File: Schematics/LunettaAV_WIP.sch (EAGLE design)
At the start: 9 parts

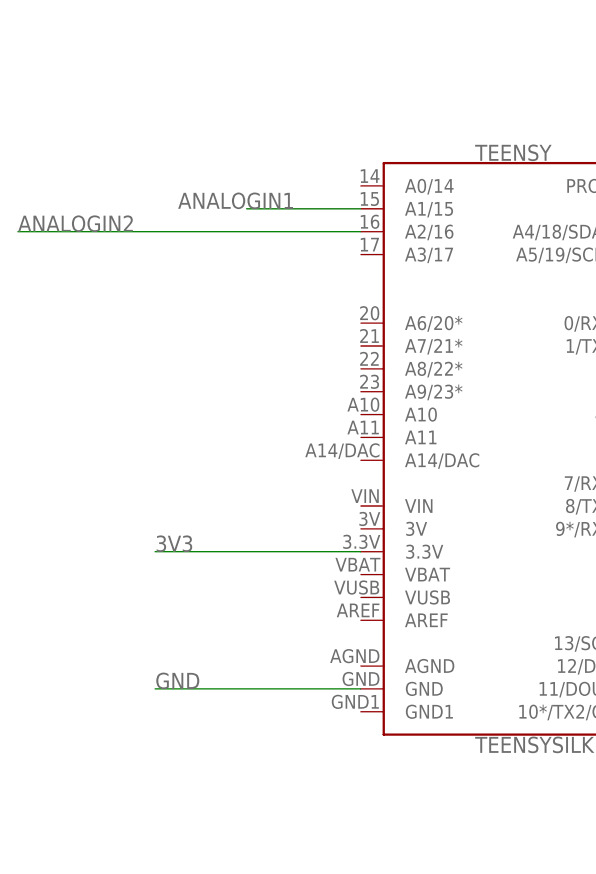
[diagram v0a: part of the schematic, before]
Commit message: fix analog input pins
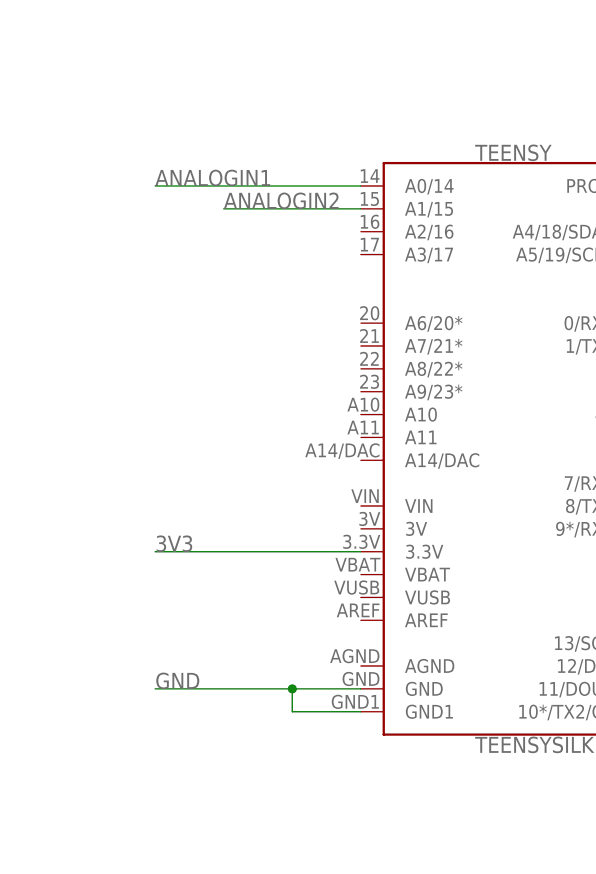
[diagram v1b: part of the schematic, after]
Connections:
- net ANALOGIN1: now also TEENSY.A0/14; no longer TEENSY.A1/15
- net ANALOGIN2: now also TEENSY.A1/15; no longer TEENSY.A2/16
- net GND: now also TEENSY.GND1
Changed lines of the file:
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@@
 <segment>
 <pinref part="TEENSY" gate="G$1" pin="GND"/>
-<wire x1="15.24" y1="25.4" x2="-7.62" y2="25.4" width="0.1524" layer="91"/>
+<wire x1="15.24" y1="25.4" x2="7.62" y2="25.4" width="0.1524" layer="91"/>
 <label x="-7.62" y="25.4" size="1.778" layer="95"/>
+<pinref part="TEENSY" gate="G$1" pin="GND1"/>
+<wire x1="7.62" y1="25.4" x2="-7.62" y2="25.4" width="0.1524" layer="91"/>
+<wire x1="15.24" y1="22.86" x2="7.62" y2="22.86" width="0.1524" layer="91"/>
+<wire x1="7.62" y1="22.86" x2="7.62" y2="25.4" width="0.1524" layer="91"/>
+<junction x="7.62" y="25.4"/>
 </segment>
 <segment>
@@
 <net name="ANALOGIN1" class="0">
 <segment>
-<pinref part="TEENSY" gate="G$1" pin="A1/15"/>
-<wire x1="15.24" y1="78.74" x2="2.54" y2="78.74" width="0.1524" layer="91"/>
-<label x="-5.08" y="78.74" size="1.778" layer="95"/>
-</segment>
-<segment>
 <pinref part="SPEEDER" gate="G$1" pin="S"/>
 <wire x1="73.66" y1="10.16" x2="73.66" y2="25.4" width="0.1524" layer="91"/>
 <label x="73.66" y="25.4" size="1.778" layer="95"/>
 </segment>
+<segment>
+<pinref part="TEENSY" gate="G$1" pin="A0/14"/>
+<wire x1="15.24" y1="81.28" x2="-7.62" y2="81.28" width="0.1524" layer="91"/>
+<label x="-7.62" y="81.28" size="1.778" layer="95"/>
+</segment>
 </net>
 <net name="ANALOGIN2" class="0">
-<segment>
-<pinref part="TEENSY" gate="G$1" pin="A2/16"/>
-<wire x1="15.24" y1="76.2" x2="-22.86" y2="76.2" width="0.1524" layer="91"/>
-<label x="-22.86" y="76.2" size="1.778" layer="95"/>
-</segment>
 <segment>
 <pinref part="SCALER" gate="G$1" pin="S"/>
@@
 <label x="106.68" y="25.4" size="1.778" layer="95"/>
 </segment>
+<segment>
+<pinref part="TEENSY" gate="G$1" pin="A1/15"/>
+<wire x1="15.24" y1="78.74" x2="0" y2="78.74" width="0.1524" layer="91"/>
+<label x="0" y="78.74" size="1.778" layer="95"/>
+</segment>
 </net>

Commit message: Add 358 and 4046 sections
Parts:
- added C1: 1uF, SparkFun-Capacitors:10NF-PTH-10MM-10000V-1-%
- added IC1: 4046N, 40xx:4046N
- added R4: 10K, MusicThingModular:RESISTOR7MM
- added TNSY5VIN: (no value), SparkFun-Retired:JUMPER-2PTH
- added U1: LM358, SparkFun-IC-Amplifiers:LM358
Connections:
- new net 5V: TNSY5VIN.1
- new net 9V: IC1P.VDD, U1G3.P$V+
- new net N$1: TEENSY.VIN, TNSY5VIN.2
- new net N$2: C1.2, IC1A.CX@2
- new net N$5: C1.1, IC1A.CX@1
- new net N$6: IC1A.R1, R4.2
- new net PLLCLOCK: IC1A.VCOOUT
- new net SPEEDYBUFF: IC1A.VCOIN, U1G1.-IN, U1G1.OUT
- net ANALOGIN1: now also U1G1.+IN
- net GND: now also IC1A.INH, IC1P.VSS, R4.1, U1G3.P$V-

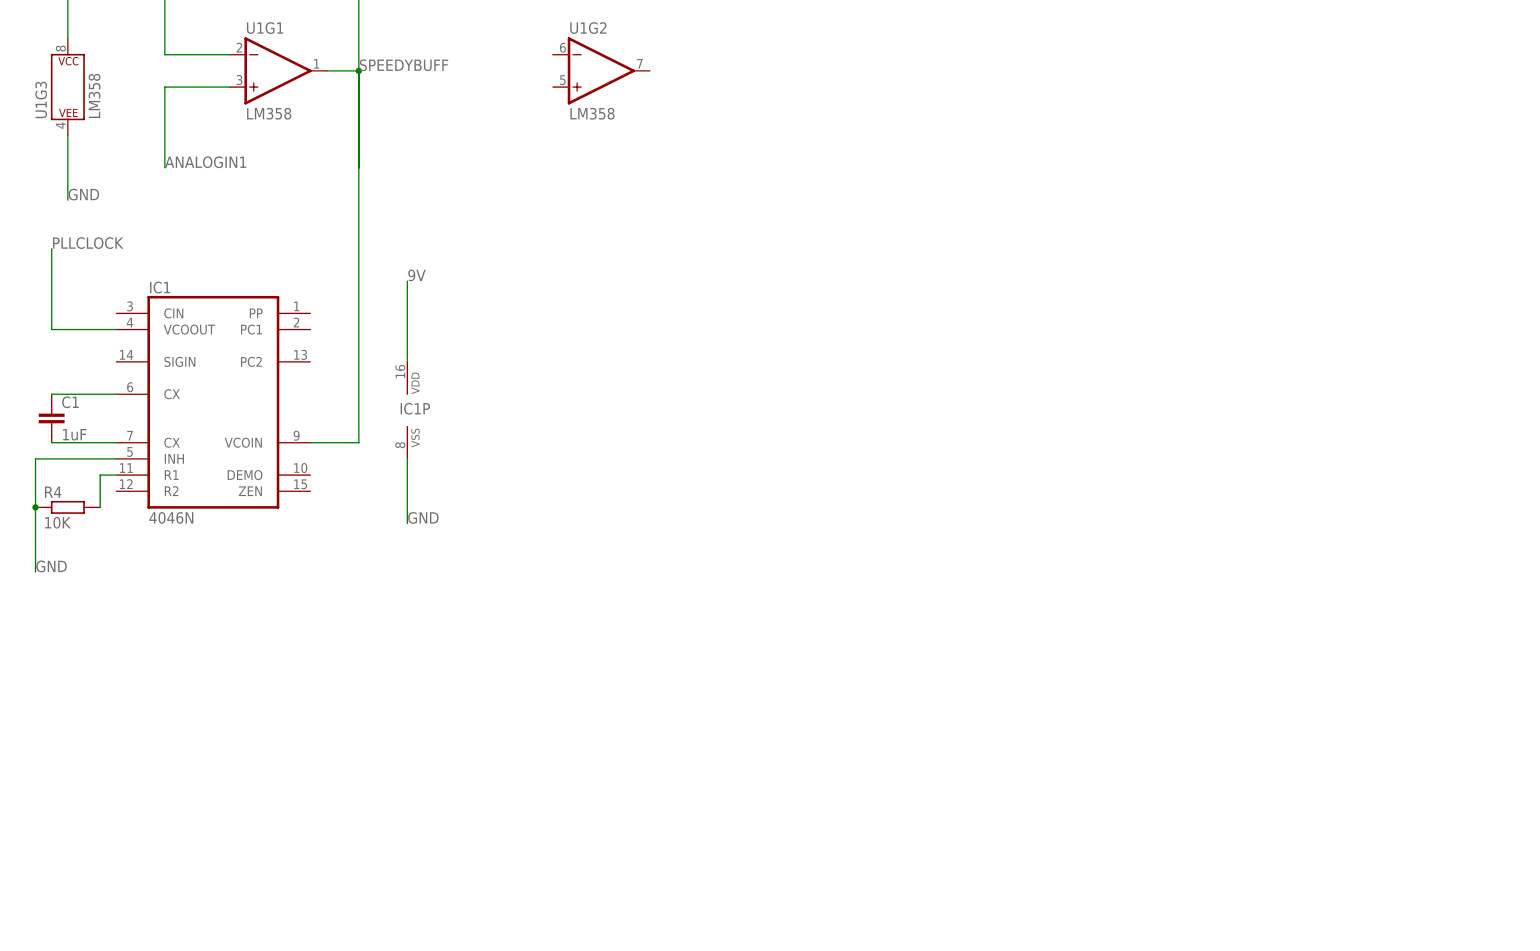
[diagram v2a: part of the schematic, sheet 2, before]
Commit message: Add compartor section
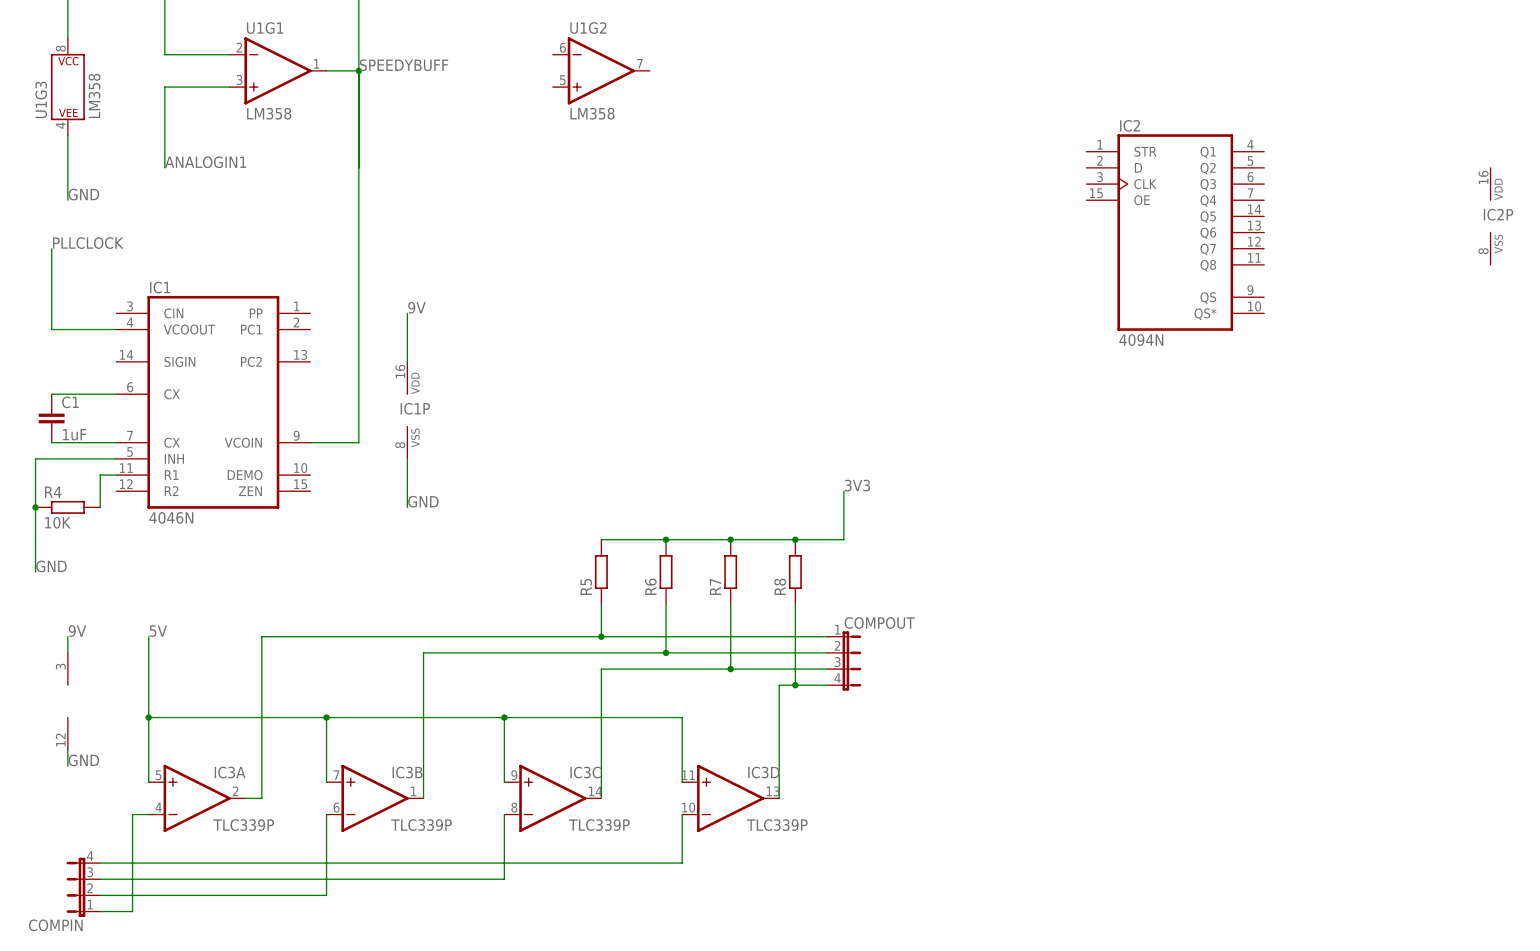
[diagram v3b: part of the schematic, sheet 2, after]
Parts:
- added COMPIN, COMPOUT: (no value), jumper:JP4E
- added IC2: 4094N, 40xx:4094N
- added IC3: TLC339P, linear:TLC339P
- added R5, R6, R7, R8: (no value), MusicThingModular:RESISTOR7MM
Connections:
- new net N$10: COMPIN.4, IC3D.-IN
- new net N$11: COMPOUT.1, IC3A.OUT, R5.1
- new net N$12: COMPOUT.2, IC3B.OUT, R6.1
- new net N$13: COMPOUT.3, IC3C.OUT, R7.1
- new net N$14: COMPOUT.4, IC3D.OUT, R8.1
- new net N$7: COMPIN.1, IC3A.-IN
- new net N$8: COMPIN.2, IC3B.-IN
- new net N$9: COMPIN.3, IC3C.-IN
- net 3V3: now also R5.2, R6.2, R7.2, R8.2
- net 5V: now also IC3A.+IN, IC3B.+IN, IC3C.+IN, IC3D.+IN
- net 9V: now also IC3P.V+
- net GND: now also IC3P.V-

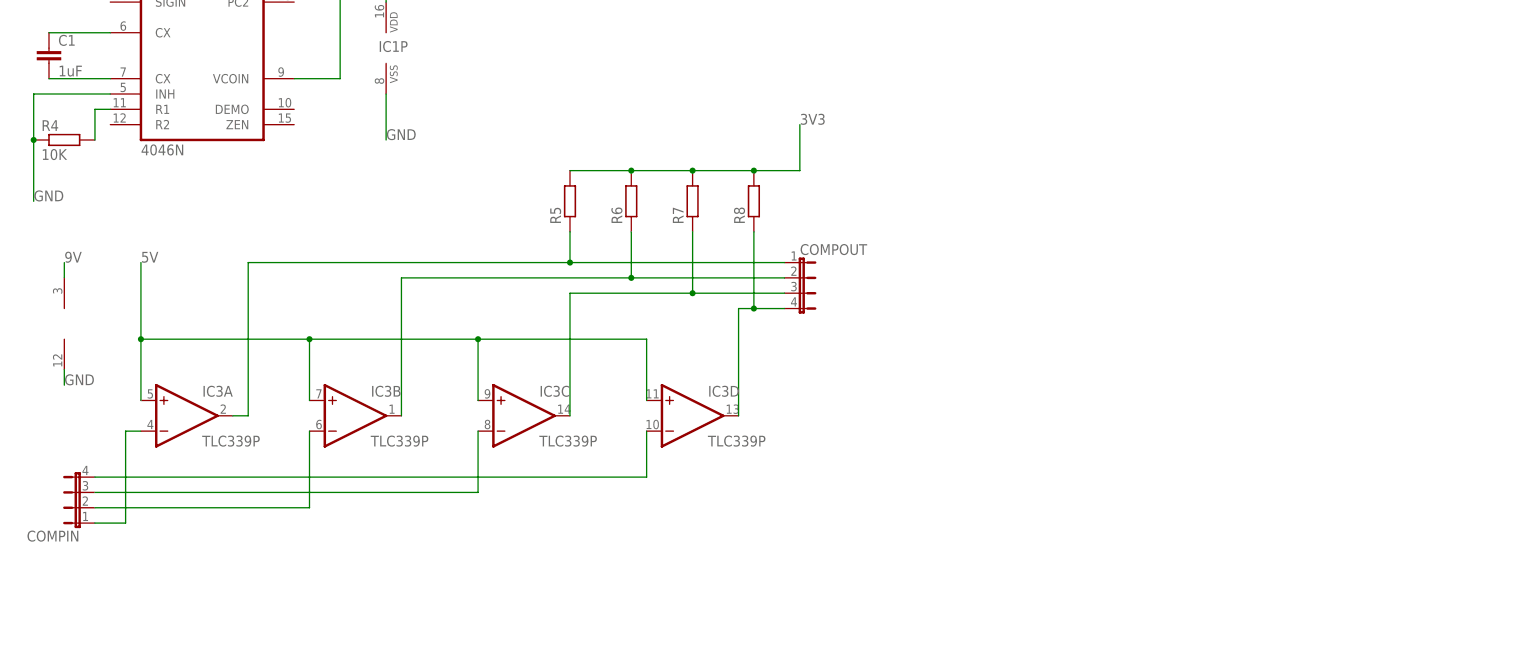
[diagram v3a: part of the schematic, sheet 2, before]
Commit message: Teensy patternSelector + schematic fixes
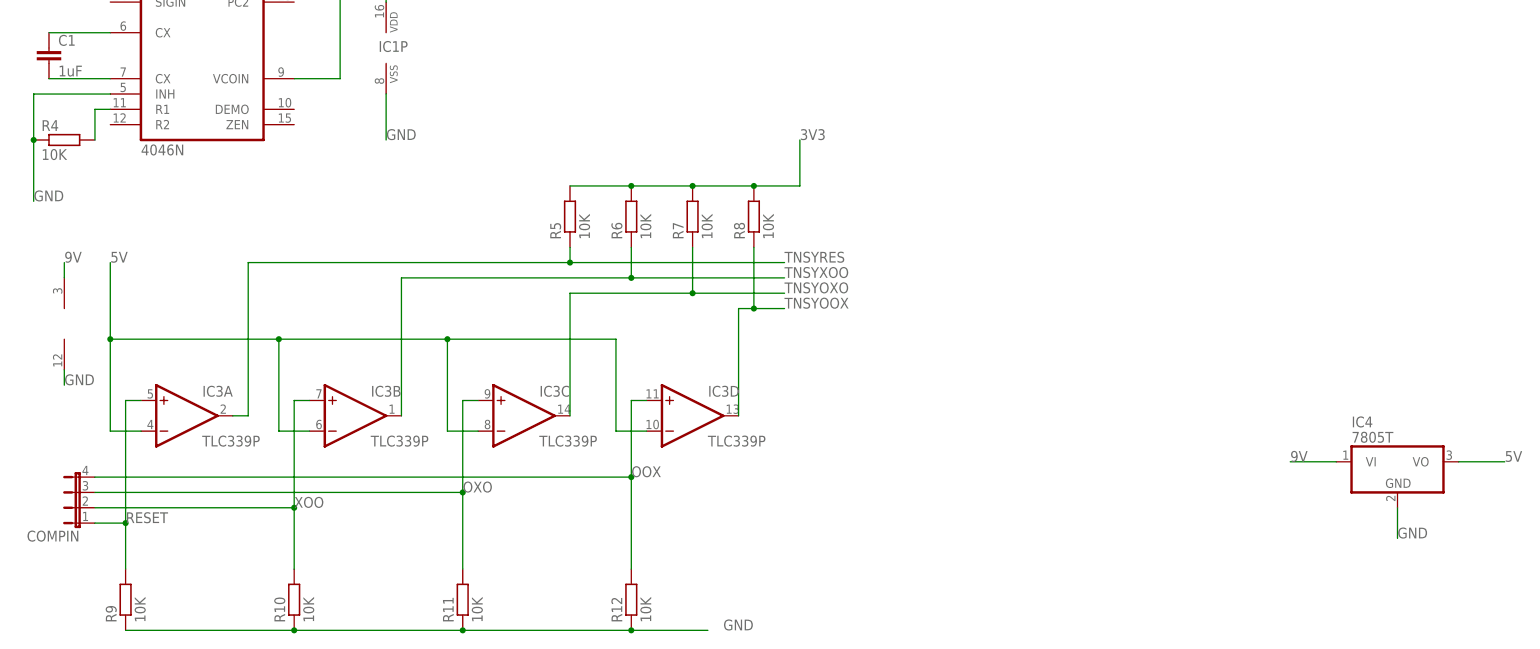
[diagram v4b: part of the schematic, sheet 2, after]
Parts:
- removed COMPOUT: (no value), jumper:JP4E
- added IC4: 7805T, linear:7805T
- added R10, R11, R12, R9: 10K, MusicThingModular:RESISTOR7MM
- R5, R6, R7, R8: value (none) -> 10K
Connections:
- removed net N$10: COMPIN.4, IC3D.-IN
- removed net N$11: COMPOUT.1, IC3A.OUT, R5.1
- removed net N$12: COMPOUT.2, IC3B.OUT, R6.1
- removed net N$13: COMPOUT.3, IC3C.OUT, R7.1
- removed net N$14: COMPOUT.4, IC3D.OUT, R8.1
- removed net N$7: COMPIN.1, IC3A.-IN
- removed net N$8: COMPIN.2, IC3B.-IN
- removed net N$9: COMPIN.3, IC3C.-IN
- new net OOX: COMPIN.4, IC3D.+IN, R12.2
- new net OXO: COMPIN.3, IC3C.+IN, R11.2
- new net RESET: COMPIN.1, IC3A.+IN, R9.2
- new net TNSYOOX: IC3D.OUT, R8.1, TEENSY.6*
- new net TNSYOXO: IC3C.OUT, R7.1, TEENSY.5*
- new net TNSYRES: IC3A.OUT, R5.1, TEENSY.3*
- new net TNSYXOO: IC3B.OUT, R6.1, TEENSY.4*
- new net XOO: COMPIN.2, IC3B.+IN, R10.2
- net 5V: now also IC3A.-IN, IC3B.-IN, IC3C.-IN, IC3D.-IN, IC4.VO; no longer IC3A.+IN, IC3B.+IN, IC3C.+IN, IC3D.+IN
- net 9V: now also IC4.VI
- net GND: now also IC4.GND, R10.1, R11.1, R12.1, R9.1
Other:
- moved on the sheet: R5, R6, R7, R8, TNSY5VIN

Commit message: Add 4094, 4017, 4040 and 4051 sections
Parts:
- added IC5: 4051N, 40xx:4051N
- added IC6: 4017N, 40xx:4017N
- added INH: 4040N, 40xx:4040N
- added JP1: (no value), jumper:JP8Q
- added JP2: (no value), jumper:JP5Q
- added PLL/X: (no value), adafruit:PINHD-1X12
- added PLLCLOCK: (no value), jumper:JP1E
- added R13: 10K, MusicThingModular:RESISTOR7MM
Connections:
- removed net PLLCLOCK: IC1A.VCOOUT
- new net AUDIORATE: IC6A.CLK
- new net BUFFCLOCK: IC2A.CLK
- new net CLOCKSELECT: JP2.1, JP2.3, JP2.5, JP2.7, JP2.9
- new net MELODYOUT: IC6A.Q0
- new net MOOX: IC5A.C
- new net MOXO: IC5A.B
- new net MXOO: IC5A.A
- new net N$11: INHA.Q5, PLL/X.5
- new net N$12: INHA.Q6, PLL/X.6
- new net N$13: INHA.Q7, PLL/X.7
- new net N$14: INHA.Q8, PLL/X.8
- new net N$15: INHA.Q9, PLL/X.9
- new net N$16: INHA.Q10, PLL/X.10
- new net N$17: INHA.Q11, PLL/X.11
- new net N$18: INHA.Q12, PLL/X.12
- new net N$19: IC5A.X, IC6A.RES
- new net N$20: IC5A.X0, IC6A.Q2
- new net N$21: IC5A.X1, IC6A.Q3
- new net N$22: IC5A.X2, IC6A.Q4
- new net N$23: IC5A.X3, IC6A.Q5
- new net N$24: IC5A.X4, IC6A.Q6
- new net N$25: IC5A.X5, IC6A.Q7
- new net N$26: IC5A.X6, IC6A.Q8
- new net N$27: IC5A.X7, IC6A.Q9
- new net N$28: IC2A.D, R13.1
- new net PLL/16: INHA.Q4, JP2.2, PLL/X.4
- new net PLL/2: INHA.Q1, JP2.8, PLL/X.1
- new net PLL/4: INHA.Q2, JP2.6, PLL/X.2
- new net PLL/8: INHA.Q3, JP2.4, PLL/X.3
- new net PLLCLOCKOUT: IC1A.VCOOUT, INHA.P1, JP2.10, PLLCLOCK.1, PLLCLOCK.2
- new net SR1: IC2A.Q1, JP1.1, JP1.2
- new net SR2: IC2A.Q2, JP1.3, JP1.4
- new net SR3: IC2A.Q3, JP1.5, JP1.6
- new net SR4: IC2A.Q4, JP1.7, JP1.8
- new net SR5: IC2A.Q5, JP1.10, JP1.9
- new net SR6: IC2A.Q6, JP1.11, JP1.12
- new net SR7: IC2A.Q7, JP1.13, JP1.14
- new net SR8: IC2A.Q8, JP1.15, JP1.16, R13.2
- net 9V: now also IC2A.STR, IC2P.VDD, IC5P.VCC, INHP.VDD
- net GND: now also IC2P.VSS, IC5P.GND, IC5P.VEE, INHP.VSS
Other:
- note added: "Use jumper to select clock rate"
- moved on the sheet: IC2, IC2P, IC4, R10, R11, R12, R5, R6, R7, R8, R9

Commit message: fix 4051 issues
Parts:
- removed PLL/X: (no value), adafruit:PINHD-1X12
- added CLOCKDIV: (no value), adafruit:PINHD-1X6
- added JP3: (no value), jumper:JP4E
- added R14, R15, R16, R17: 10K, MusicThingModular:RESISTOR7MM
- added TOTNSY: (no value), jumper:JP4Q
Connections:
- removed net N$11: INHA.Q5, PLL/X.5
- removed net N$12: INHA.Q6, PLL/X.6
- removed net N$13: INHA.Q7, PLL/X.7
- removed net N$14: INHA.Q8, PLL/X.8
- removed net N$15: INHA.Q9, PLL/X.9
- removed net N$16: INHA.Q10, PLL/X.10
- removed net N$17: INHA.Q11, PLL/X.11
- removed net N$18: INHA.Q12, PLL/X.12
- new net MINH: IC5A.INH, JP3.1, R14.1
- new net PLL/32: CLOCKDIV.5, INHA.Q5
- new net PLL/64: CLOCKDIV.6, INHA.Q6
- net GND: now also R14.2, R15.2, R16.2, R17.2
- net MOOX: now also JP3.4, R17.1
- net MOXO: now also JP3.3, R16.1
- net MXOO: now also JP3.2, R15.1
- net PLL/16: now also CLOCKDIV.4; no longer PLL/X.4
- net PLL/2: now also CLOCKDIV.1; no longer PLL/X.1
- net PLL/4: now also CLOCKDIV.2; no longer PLL/X.2
- net PLL/8: now also CLOCKDIV.3; no longer PLL/X.3
- net TNSYOOX: now also TOTNSY.1, TOTNSY.2
- net TNSYOXO: now also TOTNSY.3, TOTNSY.4
- net TNSYRES: now also TOTNSY.7, TOTNSY.8
- net TNSYXOO: now also TOTNSY.5, TOTNSY.6
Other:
- moved on the sheet: IC5, IC6, R13

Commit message: changes to schematics. brd file ignore for now.
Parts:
- removed COMPIN: (no value), jumper:JP4E
- removed NEXT: MOMENTARY-SWITCH-SPST-PTH-12MM, SparkFun-Switches:MOMENTARY-SWITCH-SPST-PTH-12MM
- removed TOTNSY: (no value), jumper:JP4Q
- added ERASE, OFFSET, WRITE: MOMENTARY-SWITCH-SPST-PTH-12MM, SparkFun-Switches:MOMENTARY-SWITCH-SPST-PTH-12MM
- added IC7: 4046N, 40xx:4046N
- added TNSYIN: (no value), jumper:JP4Q
- TEENSY: value TEENSYSILK -> TEENSYNOSILK; device SparkFun-Boards:TEENSYSILK -> SparkFun-Boards:TEENSYNOSILK
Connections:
- net 3V3: now also OFFSET.1; no longer NEXT.2
- net 9V: now also IC7P.VDD, WRITE.1
- net BUFFCLOCK: now also U1G2.-IN, U1G2.OUT
- net CLOCKSELECT: now also U1G2.+IN
- net DIN1: now also OFFSET.2; no longer NEXT.1
- net GND: now also ERASE.1, IC7A.INH, IC7P.VSS; no longer IC1A.INH
- net N$2: now also IC7A.CX@2; no longer IC1A.CX@2
- net N$28: now also ERASE.2, WRITE.2
- net N$5: now also IC7A.CX@1; no longer IC1A.CX@1
- net N$6: now also IC7A.R1; no longer IC1A.R1
- net OOX: now also TNSYIN.1, TNSYIN.2; no longer COMPIN.4
- net OXO: now also TNSYIN.3, TNSYIN.4; no longer COMPIN.3
- net PLLCLOCKOUT: now also IC7A.VCOOUT; no longer IC1A.VCOOUT
- net RESET: now also TNSYIN.7, TNSYIN.8; no longer COMPIN.1
- net SPEEDYBUFF: now also IC7A.VCOIN; no longer IC1A.VCOIN
- net TNSYOOX: no longer TOTNSY.1, TOTNSY.2
- net TNSYOXO: no longer TOTNSY.3, TOTNSY.4
- net TNSYRES: no longer TOTNSY.7, TOTNSY.8
- net TNSYXOO: no longer TOTNSY.5, TOTNSY.6
- net XOO: now also TNSYIN.5, TNSYIN.6; no longer COMPIN.2
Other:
- moved on the sheet: IC1P, IC2, IC2P, IC5, IC5P, IC6, JP1, JP3, OLED1, OLED2, R1, R13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
